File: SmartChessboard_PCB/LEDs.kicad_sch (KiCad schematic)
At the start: 82 parts, among them U7 74LVC1T45DW-7

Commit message: before hall sensors
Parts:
- removed C13, C14, C15, C16, C17, C18, C19, C20, C21, C22, C23, C24, C25, C26, C27, C28, C29, C30, C31, C32, C33, C34, C35, C36, C37, C38, C39, C40, C41, C42, C43, C44, C45, C46, C47, C48, C49, C50, C51, C52, C53, C54, C55, C56, C57, C58, C59, C60, C61, C62, C63, C64, C65, C66, C67, C68, C69, C70, C71, C72, C73, C74, C75, C76, C77: 100n, CAP 0805, symbol ChessBoardSchLib:root_1_CAP 0805_ChessBoardSchLib.SchLib
- removed D? (x16): WS2812B, PCM_JLCPCB:LED_WS2812B_PLCC4_5.0x5.0mm_P3.2mm, symbol PCM_JLCPCB-Extended:LED, WS2812B, 5050
- removed U7: 74LVC1T45DW-7, 74LVC1T45DW-7, symbol ChessBoardSchLib:root_0_74LVC1T45DW-7_ChessBoardSchLib.SchLib
- added C14, C15, C16, C17, C18, C19, C20, C21, C22, C23, C24, C25, C26, C27, C28, C29, C30, C31, C32, C33, C34, C35, C36, C37, C38, C39, C40, C41, C42, C43, C44, C45, C46, C47, C48, C49, C50, C51, C52, C53, C54, C55, C56, C57, C58, C59, C60, C61, C62, C63, C64, C65, C66, C67, C68, C69, C70, C71, C72, C73, C74, C75, C76, C77: 100nF, PCM_JLCPCB:C_0402, symbol PCM_JLCPCB-Capacitors:0402,100nF,(2)
- added D10, D11, D12, D13, D14, D15, D16, D17, D18, D19, D20, D21, D22, D23, D24, D25, D26, D27, D28, D29, D30, D31, D32, D33, D34, D35, D36, D37, D38, D39, D40, D41, D42, D43, D44, D45, D46, D47, D48, D49, D50, D51, D52, D53, D54, D55, D56, D57, D58, D59, D60, D61, D62, D63, D64, D65, D66, D67, D68, D69, D7, D70, D8, D9: WS2812B, LED_SMD:LED_WS2812B_PLCC4_5.0x5.0mm_P3.2mm, symbol LED:WS2812B
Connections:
- net +5V: now also C14.1, C15.1, C16.1, C17.1, C18.1, C19.1, C20.1, C21.1, C22.1, C23.1, C24.1, C25.1, C26.1, C27.1, C28.1, C29.1, C30.1, C31.1, C32.1, C33.1, C34.1, C35.1, C36.1, C37.1, C38.1, C39.1, C40.1, C41.1, C42.1, C43.1, C44.1, C45.1, C46.1, C47.1, C48.1, C49.1, C50.1, C51.1, C52.1, C53.1, C54.1, C55.1, C56.1, C57.1, C58.1, C59.1, C60.1, C61.1, C62.1, C63.1, C64.1, C65.1, C66.1, C67.1, C68.1, C69.1, C70.1, C71.1, C72.1, C73.1, C74.1, C75.1, C76.1, C77.1, D10.1 (VDD), D11.1 (VDD), D12.1 (VDD), D13.1 (VDD), D14.1 (VDD), D15.1 (VDD), D16.1 (VDD), D17.1 (VDD), D18.1 (VDD), D19.1 (VDD), D20.1 (VDD), D21.1 (VDD), D22.1 (VDD), D23.1 (VDD), D24.1 (VDD), D25.1 (VDD), D26.1 (VDD), D27.1 (VDD), D28.1 (VDD), D29.1 (VDD), D30.1 (VDD), D31.1 (VDD), D32.1 (VDD), D33.1 (VDD), D34.1 (VDD), D35.1 (VDD), D36.1 (VDD), D37.1 (VDD), D38.1 (VDD), D39.1 (VDD), D40.1 (VDD), D41.1 (VDD), D42.1 (VDD), D43.1 (VDD), D44.1 (VDD), D45.1 (VDD), D46.1 (VDD), D47.1 (VDD), D48.1 (VDD), D49.1 (VDD), D50.1 (VDD), D51.1 (VDD), D52.1 (VDD), D53.1 (VDD), D54.1 (VDD), D55.1 (VDD), D56.1 (VDD), D57.1 (VDD), D58.1 (VDD), D59.1 (VDD), D60.1 (VDD), D61.1 (VDD), D62.1 (VDD), D63.1 (VDD), D64.1 (VDD), D65.1 (VDD), D66.1 (VDD), D67.1 (VDD), D68.1 (VDD), D69.1 (VDD), D7.1 (VDD), D70.1 (VDD), D8.1 (VDD), D9.1 (VDD)
- net GND: now also C14.2, C15.2, C16.2, C17.2, C18.2, C19.2, C20.2, C21.2, C22.2, C23.2, C24.2, C25.2, C26.2, C27.2, C28.2, C29.2, C30.2, C31.2, C32.2, C33.2, C34.2, C35.2, C36.2, C37.2, C38.2, C39.2, C40.2, C41.2, C42.2, C43.2, C44.2, C45.2, C46.2, C47.2, C48.2, C49.2, C50.2, C51.2, C52.2, C53.2, C54.2, C55.2, C56.2, C57.2, C58.2, C59.2, C60.2, C61.2, C62.2, C63.2, C64.2, C65.2, C66.2, C67.2, C68.2, C69.2, C70.2, C71.2, C72.2, C73.2, C74.2, C75.2, C76.2, C77.2, D10.3 (VSS), D11.3 (VSS), D12.3 (VSS), D13.3 (VSS), D14.3 (VSS), D15.3 (VSS), D16.3 (VSS), D17.3 (VSS), D18.3 (VSS), D19.3 (VSS), D20.3 (VSS), D21.3 (VSS), D22.3 (VSS), D23.3 (VSS), D24.3 (VSS), D25.3 (VSS), D26.3 (VSS), D27.3 (VSS), D28.3 (VSS), D29.3 (VSS), D30.3 (VSS), D31.3 (VSS), D32.3 (VSS), D33.3 (VSS), D34.3 (VSS), D35.3 (VSS), D36.3 (VSS), D37.3 (VSS), D38.3 (VSS), D39.3 (VSS), D40.3 (VSS), D41.3 (VSS), D42.3 (VSS), D43.3 (VSS), D44.3 (VSS), D45.3 (VSS), D46.3 (VSS), D47.3 (VSS), D48.3 (VSS), D49.3 (VSS), D50.3 (VSS), D51.3 (VSS), D52.3 (VSS), D53.3 (VSS), D54.3 (VSS), D55.3 (VSS), D56.3 (VSS), D57.3 (VSS), D58.3 (VSS), D59.3 (VSS), D60.3 (VSS), D61.3 (VSS), D62.3 (VSS), D63.3 (VSS), D64.3 (VSS), D65.3 (VSS), D66.3 (VSS), D67.3 (VSS), D68.3 (VSS), D69.3 (VSS), D7.3 (VSS), D70.3 (VSS), D8.3 (VSS), D9.3 (VSS)
- net LED_OUT_1: now also D35.2 (DOUT), D8.4 (DIN)
- net LED_OUT_2: now also D36.2 (DOUT), D9.4 (DIN)
- net LED_OUT_3: now also D10.4 (DIN), D37.2 (DOUT)
- net LED_OUT_4: now also D38.2 (DOUT), D39.4 (DIN)
- net LED_OUT_5: now also D40.4 (DIN), D67.2 (DOUT)
- net LED_OUT_6: now also D41.4 (DIN), D68.2 (DOUT)
- net LED_OUT_7: now also D42.4 (DIN), D69.2 (DOUT)
- new net: D34.2 (DOUT), D38.4 (DIN)
- new net: D66.2 (DOUT), D70.4 (DIN)
- new net: D42.2 (DOUT), D46.4 (DIN)
- new net: D65.2 (DOUT), D69.4 (DIN)
- new net: D11.2 (DOUT), D15.4 (DIN)
- new net: D11.4 (DIN), D7.2 (DOUT)
- new net: D28.2 (DOUT), D32.4 (DIN)
- new net: D24.2 (DOUT), D28.4 (DIN)
- new net: D31.2 (DOUT), D35.4 (DIN)
- new net: D27.2 (DOUT), D31.4 (DIN)
- new net: D18.2 (DOUT), D22.4 (DIN)
- new net: D14.2 (DOUT), D18.4 (DIN)
- new net: D23.2 (DOUT), D27.4 (DIN)
- new net: D64.2 (DOUT), D68.4 (DIN)
- new net: D16.2 (DOUT), D20.4 (DIN)
- new net: D12.2 (DOUT), D16.4 (DIN)
- new net: D22.2 (DOUT), D26.4 (DIN)
- new net: D41.2 (DOUT), D45.4 (DIN)
- new net: D46.2 (DOUT), D50.4 (DIN)
- new net: D26.2 (DOUT), D30.4 (DIN)
- new net: D49.2 (DOUT), D53.4 (DIN)
- new net: D45.2 (DOUT), D49.4 (DIN)
- new net: D30.2 (DOUT), D34.4 (DIN)
- new net: D56.2 (DOUT), D60.4 (DIN)
- new net: D52.2 (DOUT), D56.4 (DIN)
- new net: D61.2 (DOUT), D65.4 (DIN)
- new net: D60.2 (DOUT), D64.4 (DIN)
- new net: D58.2 (DOUT), D62.4 (DIN)
- new net: D54.2 (DOUT), D58.4 (DIN)
- new net: D57.2 (DOUT), D61.4 (DIN)
- new net: D13.2 (DOUT), D17.4 (DIN)
- new net: D13.4 (DIN), D9.2 (DOUT)
- new net: D59.2 (DOUT), D63.4 (DIN)
- new net: D55.2 (DOUT), D59.4 (DIN)
- new net: D47.2 (DOUT), D51.4 (DIN)
- new net: D43.2 (DOUT), D47.4 (DIN)
- new net: D63.2 (DOUT), D67.4 (DIN)
- new net: D20.2 (DOUT), D24.4 (DIN)
- new net: D51.2 (DOUT), D55.4 (DIN)
- new net: D12.4 (DIN), D8.2 (DOUT)
- new net: D53.2 (DOUT), D57.4 (DIN)
- new net: D48.2 (DOUT), D52.4 (DIN)
- new net: D25.2 (DOUT), D29.4 (DIN)
- new net: D21.2 (DOUT), D25.4 (DIN)
- new net: D32.2 (DOUT), D36.4 (DIN)
- new net: D29.2 (DOUT), D33.4 (DIN)
- new net: D50.2 (DOUT), D54.4 (DIN)
- new net: D44.2 (DOUT), D48.4 (DIN)
- new net: D15.2 (DOUT), D19.4 (DIN)
- new net: D19.2 (DOUT), D23.4 (DIN)
- new net: D10.2 (DOUT), D14.4 (DIN)
- new net: D33.2 (DOUT), D37.4 (DIN)
- new net: D39.2 (DOUT), D43.4 (DIN)
- new net: D40.2 (DOUT), D44.4 (DIN)
- new net: D17.2 (DOUT), D21.4 (DIN)
- new net: D62.2 (DOUT), D66.4 (DIN)
- new net ESP46/LED: D7.4 (DIN)
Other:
- note removed: "Level Shifter"

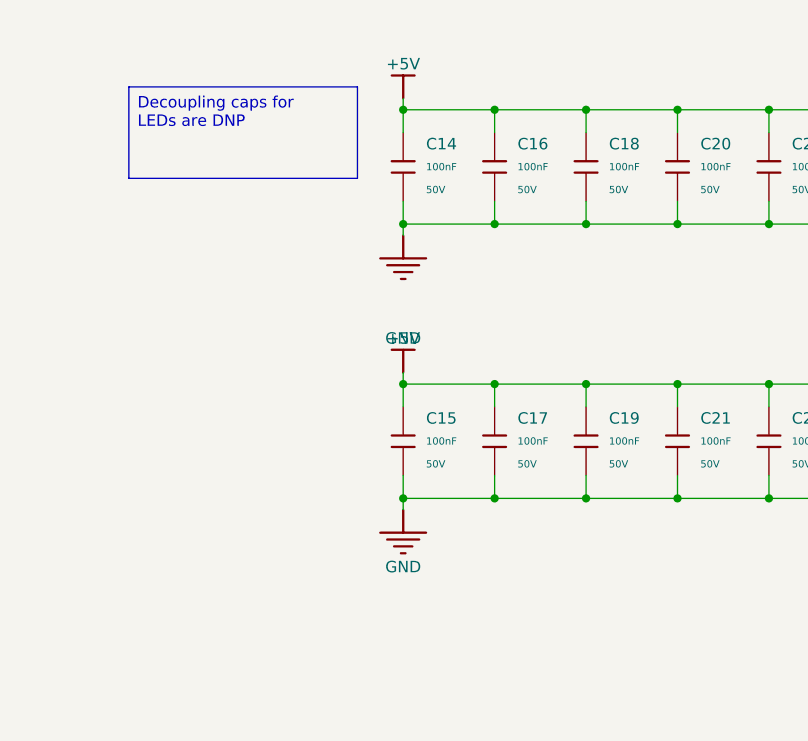
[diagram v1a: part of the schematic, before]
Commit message: level shifter added
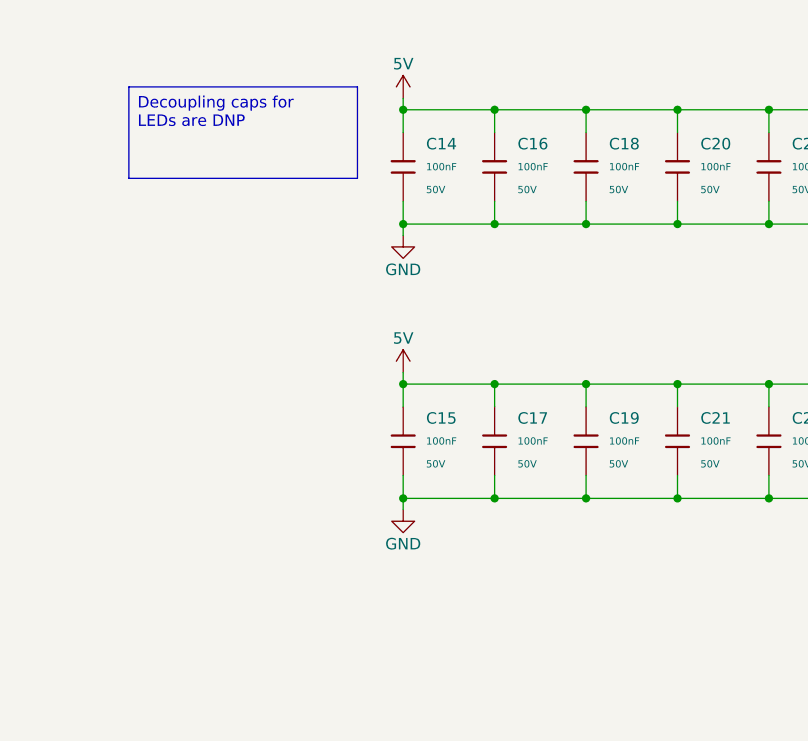
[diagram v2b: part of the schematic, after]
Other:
- title: (none) -> SmartChessboard

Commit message: psc
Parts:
- added Q1: BSS138, Package_TO_SOT_SMD:SOT-23, symbol Transistor_FET:BSS138
- added R89, R90: 10k, SparkFun-Resistor:R_0402_1005Metric, symbol SparkFun-Resistor:10k_0402
- renumbered C14 to C12, C15 to C13, C16 to C14, C17 to C15, C18 to C16, C19 to C17, C20 to C18, C21 to C19, C22 to C20, C23 to C21, C24 to C22, C25 to C23, C26 to C24, C27 to C25, C28 to C26, C29 to C27, C30 to C28, C31 to C29, C32 to C30, C33 to C31, C34 to C32, C35 to C33, C36 to C34, C37 to C35, C38 to C36, C39 to C37, C40 to C38, C41 to C39, C42 to C40, C43 to C41, C44 to C42, C45 to C43, C46 to C44, C47 to C45, C48 to C46, C49 to C47, C50 to C48, C51 to C49, C52 to C50, C53 to C51, C54 to C52, C55 to C53, C56 to C54, C57 to C55, C58 to C56, C59 to C57, C60 to C58, C61 to C59, C62 to C60, C63 to C61, C64 to C62, C65 to C63, C66 to C64, C67 to C65, C68 to C66, C69 to C67, C70 to C68, C71 to C69, C72 to C70, C73 to C71, C74 to C72, C75 to C73, C76 to C74, C77 to C75, D11 to D10, D12 to D11, D13 to D12, D14 to D13, D15 to D14, D16 to D15, D17 to D16, D18 to D17, D19 to D18, D20 to D19, D21 to D20, D22 to D21, D23 to D22, D24 to D23, D25 to D24, D26 to D25, D27 to D26, D28 to D27, D29 to D28, D30 to D29, D31 to D30, D32 to D31, D33 to D32, D34 to D33, D35 to D34, D36 to D35, D37 to D36, D38 to D37, D39 to D38, D40 to D39, D41 to D40, D42 to D41, D43 to D42, D44 to D43, D45 to D44, D46 to D45, D47 to D46, D48 to D47, D49 to D48, D50 to D49, D51 to D50, D52 to D51, D53 to D52, D54 to D53, D55 to D54, D56 to D55, D57 to D56, D58 to D57, D59 to D58, D60 to D59, D7 to D6, D61 to D60, D62 to D61, D63 to D62, D64 to D63, D65 to D64, D66 to D65, D67 to D66, D68 to D67, D69 to D68, D70 to D69, D8 to D7, D9 to D8, D10 to D9
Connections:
- net +5V: now also R90.1
- net ESP46/LED: now also Q1.2 (S), R89.2; no longer D6.4 (DIN)
- new net 3.3V: Q1.1 (G), R89.1
- new net HV_ESP46/LED: D6.4 (DIN), Q1.3 (D), R90.2
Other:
- note added: "Bidirectional Logic Level Converter"
- moved on the sheet: D10, D11, D12, D13, D14, D15, D16, D17, D18, D19, D20, D21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
